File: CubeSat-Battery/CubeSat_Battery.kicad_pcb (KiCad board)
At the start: 2 copper layers, 92 x 92 mm, 8 parts, among them J1 Conn_01x02_Pin, J6 Screw_Terminal_01x02, U1 BatteryPack

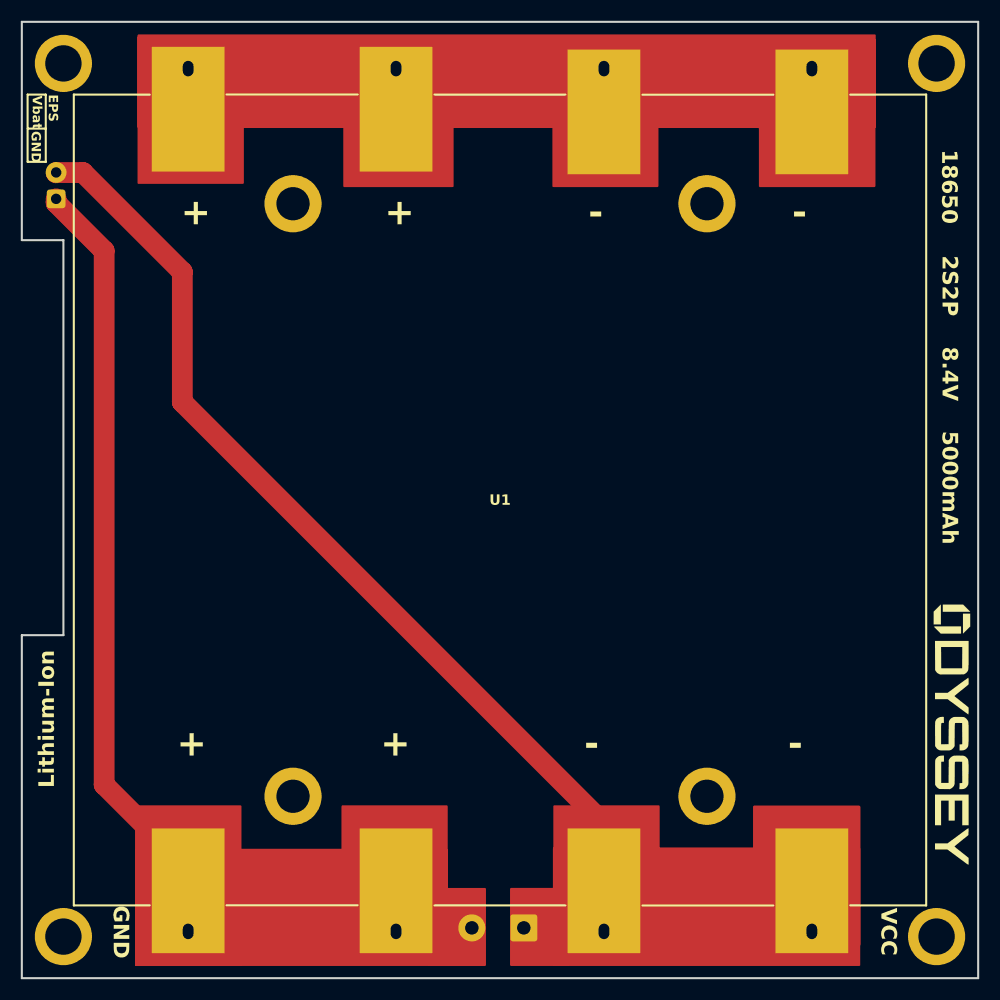
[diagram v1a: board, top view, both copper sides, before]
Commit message: changing the size of the vias
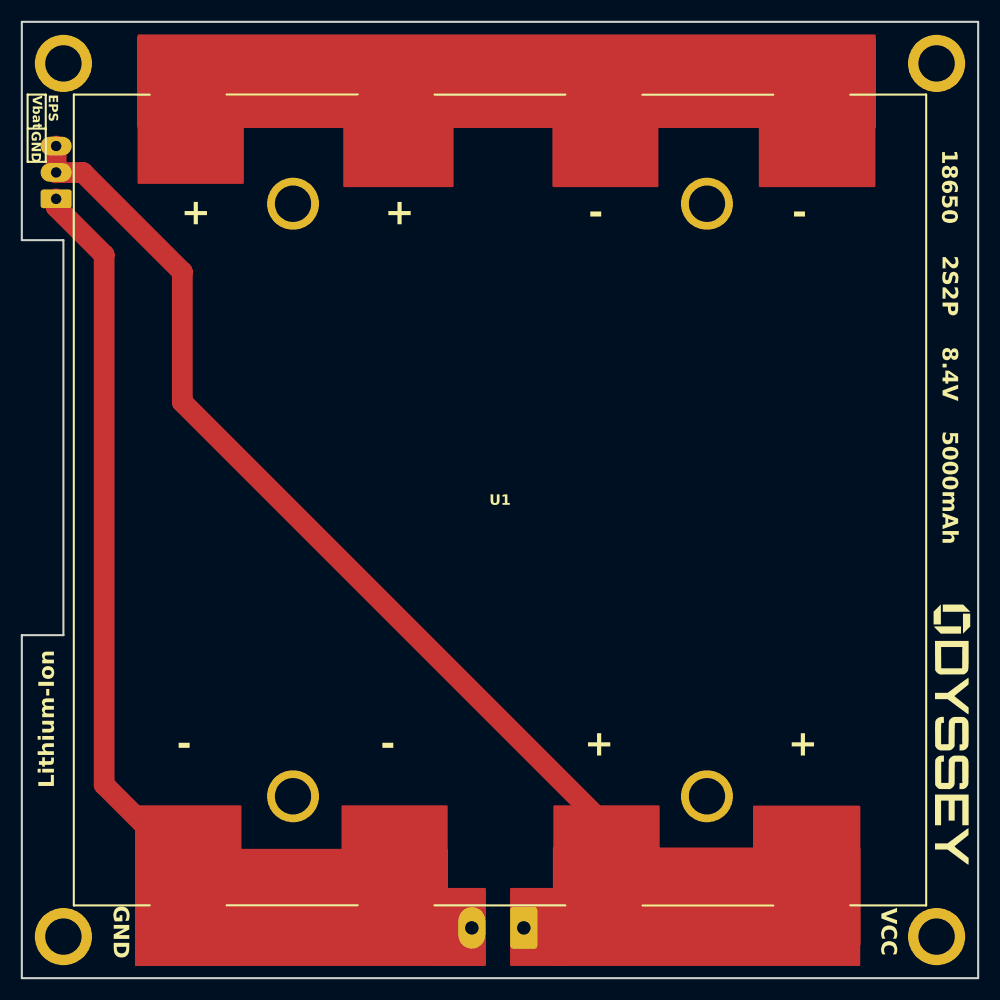
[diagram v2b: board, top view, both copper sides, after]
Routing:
- net Vbat_8.4V: track 96.8 -> 99.4 mm
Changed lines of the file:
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@@
 		(pad "" thru_hole circle
 			(at -19.91 -28.5)
-			(size 5.5 5.5)
-			(drill 3.2)
+			(size 5 5)
+			(drill 3.5)
 			(layers "*.Cu" "*.Mask")
 			(remove_unused_layers no)
@@
 		(pad "" thru_hole circle
 			(at -19.91 28.5)
-			(size 5.5 5.5)
-			(drill 3.2)
+			(size 5 5)
+			(drill 3.5)
 			(layers "*.Cu" "*.Mask")
 			(remove_unused_layers no)
@@
 		(pad "" thru_hole circle
 			(at 19.91 -28.5)
-			(size 5.5 5.5)
-			(drill 3.2)
+			(size 5 5)
+			(drill 3.5)
 			(layers "*.Cu" "*.Mask")
 			(remove_unused_layers no)
@@
 		(pad "" thru_hole circle
 			(at 19.91 28.5)
-			(size 5.5 5.5)
-			(drill 3.2)
+			(size 5 5)
+			(drill 3.5)
 			(layers "*.Cu" "*.Mask")
 			(remove_unused_layers no)
 			(zone_connect 2)
 		)
-		(pad "1" thru_hole rect
+		(pad "1" smd rect
 			(at -30 -41.5 90)
 			(size 12 7)
-			(drill oval 1.5 1.04
+			(drill oval
 				(offset -3.905 0)
 			)
-			(layers "*.Cu" "*.Mask")
-			(remove_unused_layers no)
+			(layers "F.Cu" "F.Mask" "F.Paste")
 			(net 1 "Vcell_4.2V")
 			(pinfunction "P1")
@@
 			(solder_mask_margin 0.102)
 		)
-		(pad "2" thru_hole rect
+		(pad "2" smd rect
 			(at -10 -41.5 90)
 			(size 12 7)
-			(drill oval 1.5 1.04
+			(drill oval
 				(offset -3.905 0)
 			)
-			(layers "*.Cu" "*.Mask")
-			(remove_unused_layers no)
+			(layers "F.Cu" "F.Mask" "F.Paste")
 			(net 1 "Vcell_4.2V")
 			(pinfunction "P2")
@@
 			(solder_mask_margin 0.102)
 		)
-		(pad "3" thru_hole rect
+		(pad "3" smd rect
 			(at 10 -41.5 90)
 			(size 12 7)
-			(drill oval 1.5 1.04
-				(offset -4.165001 0)
-			)
-			(layers "*.Cu" "*.Mask")
-			(remove_unused_layers no)
+			(drill oval
+				(offset -3.905 0)
+			)
+			(layers "F.Cu" "F.Mask" "F.Paste")
 			(net 1 "Vcell_4.2V")
 			(pinfunction "P3")
@@
 			(solder_mask_margin 0.102)
 		)
-		(pad "4" thru_hole rect
+		(pad "4" smd rect
 			(at 30 -41.5 90)
 			(size 12 7)
-			(drill oval 1.5 1.04
+			(drill oval
 				(offset -4.165001 0)
 			)
-			(layers "*.Cu" "*.Mask")
-			(remove_unused_layers no)
+			(layers "F.Cu" "F.Mask" "F.Paste")
 			(net 1 "Vcell_4.2V")
 			(pinfunction "P4")
@@
 			(solder_mask_margin 0.102)
 		)
-		(pad "5" thru_hole rect
+		(pad "5" smd rect
 			(at -30 41.5 90)
 			(size 12 7)
-			(drill oval 1.5 1.04
+			(drill oval
 				(offset 3.905 0)
 			)
-			(layers "*.Cu" "*.Mask")
-			(remove_unused_layers no)
+			(layers "F.Cu" "F.Mask" "F.Paste")
 			(net 3 "GND")
 			(pinfunction "P5")
@@
 			(solder_mask_margin 0.102)
 		)
-		(pad "6" thru_hole rect
+		(pad "6" smd rect
 			(at -10 41.5 90)
 			(size 12 7)
-			(drill oval 1.5 1.04
+			(drill oval
 				(offset 3.905 0)
 			)
-			(layers "*.Cu" "*.Mask")
-			(remove_unused_layers no)
+			(layers "F.Cu" "F.Mask" "F.Paste")
 			(net 3 "GND")
 			(pinfunction "P6")
@@
 			(solder_mask_margin 0.102)
 		)
-		(pad "7" thru_hole rect
+		(pad "7" smd rect
 			(at 10 41.5 90)
 			(size 12 7)
-			(drill oval 1.5 1.04
+			(drill oval
 				(offset 3.905 0)
 			)
-			(layers "*.Cu" "*.Mask")
-			(remove_unused_layers no)
+			(layers "F.Cu" "F.Mask" "F.Paste")
 			(net 2 "Vbat_8.4V")
 			(pinfunction "P7")
@@
 			(solder_mask_margin 0.102)
 		)
-		(pad "8" thru_hole rect
+		(pad "8" smd rect
 			(at 30 41.5 90)
 			(size 12 7)
-			(drill oval 1.5 1.04
+			(drill oval
 				(offset 3.905 0)
 			)
-			(layers "*.Cu" "*.Mask")
-			(remove_unused_layers no)
+			(layers "F.Cu" "F.Mask" "F.Paste")
 			(net 2 "Vbat_8.4V")
 			(pinfunction "P8")
@@
 		(pad "1" thru_hole roundrect
 			(at 0 0 180)
-			(size 2.6 2.6)
+			(size 2.6 4)
 			(drill 1.3)
 			(layers "*.Cu" "*.Mask")
@@
 			(pintype "passive")
 		)
-		(pad "2" thru_hole circle
+		(pad "2" thru_hole oval
 			(at 5 0 180)
-			(size 2.6 2.6)
+			(size 2.6 4)
 			(drill 1.3)
 			(layers "*.Cu" "*.Mask")
@@
 		)
 		(property "Value" "Conn_01x02_Pin"
-			(at -5.05 42.34 270)
+			(at -5.05 42.34 90)
 			(layer "B.Fab")
 			(effects
@@
 		)
 		(property "Datasheet" "~"
-			(at 0 0 270)
+			(at 0 0 90)
 			(layer "B.Fab")
 			(hide yes)
@@
 		)
 		(property "Description" "Generic connector, single row, 01x02, script generated"
-			(at 0 0 270)
+			(at 0 0 90)
 			(layer "B.Fab")
 			(hide yes)
@@
 		)
 		(fp_text user "${REFERENCE}"
-			(at 1.25 -1.5 270)
+			(at 1.25 -1.5 90)
 			(layer "B.Fab")
 			(effects
@@
 		(pad "1" thru_hole roundrect
 			(at 0 0 90)
-			(size 1.8 1.8)
+			(size 1.8 3)
 			(drill 1)
 			(layers "*.Cu" "*.Mask")
@@
 		(pad "2" thru_hole oval
 			(at 2.54 0 90)
-			(size 2 2)
+			(size 1.8 3)
 			(drill 1)
 			(layers "*.Cu" "*.Mask")
@@
 			(pintype "passive")
 		)
+		(pad "2" thru_hole oval
+			(at 5.08 0 90)
+			(size 1.8 3)
+			(drill 1)
+			(layers "*.Cu" "*.Mask")
+			(remove_unused_layers no)
+			(net 2 "Vbat_8.4V")
+			(pinfunction "Pin_2")
+			(pintype "passive")
+		)
 		(embedded_fonts no)
 		(model "${KICAD9_3DMODEL_DIR}/Connector_JST.3dshapes/JST_EH_B2B-EH-A_1x02_P2.50mm_Vertical.step"
@@
 		(layer "Edge.Cuts")
 	)
-	(gr_text "-"
+	(gr_text "+"
 		(at 73.7 -21.11 0)
 		(layer "F.SilkS")
@@
 		)
 	)
-	(gr_text "-"
+	(gr_text "+"
 		(at 54.1 -21.11 0)
 		(layer "F.SilkS")
@@
 		)
 	)
-	(gr_text "+"
+	(gr_text "-"
 		(at 34.5 -21.11 0)
 		(layer "F.SilkS")
@@
 		)
 	)
-	(gr_text "+"
+	(gr_text "-"
 		(at 14.9 -21.11 0)
 		(layer "F.SilkS")
@@
 	)
 	(segment
+		(start 3.3 -77.51)
+		(end 3.3 -80.05)
+		(width 2)
+		(layer "F.Cu")
+		(net 2)
+	)
+	(segment
 		(start 3.33 -77.5)
 		(end 5.88 -77.5)
@@
 	)
 	(segment
-		(start 3.3 -74.59)
-		(end 7.92 -69.97)
-		(width 2)
-		(layer "F.Cu")
-		(net 3)
-	)
-	(segment
-		(start 7.92 -69.97)
-		(end 7.92 -18.61)
-		(width 2)
-		(layer "F.Cu")
-		(net 3)
-	)
-	(segment
 		(start 3.3 -74.97)
-		(end 3.3 -74.59)
+		(end 3.3 -74.2)
 		(width 2)
 		(layer "F.Cu")
@@
 	)
 	(segment
+		(start 7.92 -69.58)
+		(end 7.92 -18.61)
+		(width 2)
+		(layer "F.Cu")
+		(net 3)
+	)
+	(segment
 		(start 16 -10.53)
 		(end 16 -4.5)
 		(width 2)
 		(layer "F.Cu")
+		(net 3)
+	)
+	(segment
+		(start 3.3 -74.2)
+		(end 7.92 -69.58)
+		(width 2)
+		(layer "F.Cu")
